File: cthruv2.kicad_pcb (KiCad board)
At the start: 6 copper layers, 27 x 16.4 mm, 10 parts, among them J1 USB_C_Receptacle, J2 Conn_01x03, J3 Conn_01x05, J7 VBUS, J8 Conn_01x05, P1 USB_C_Plug

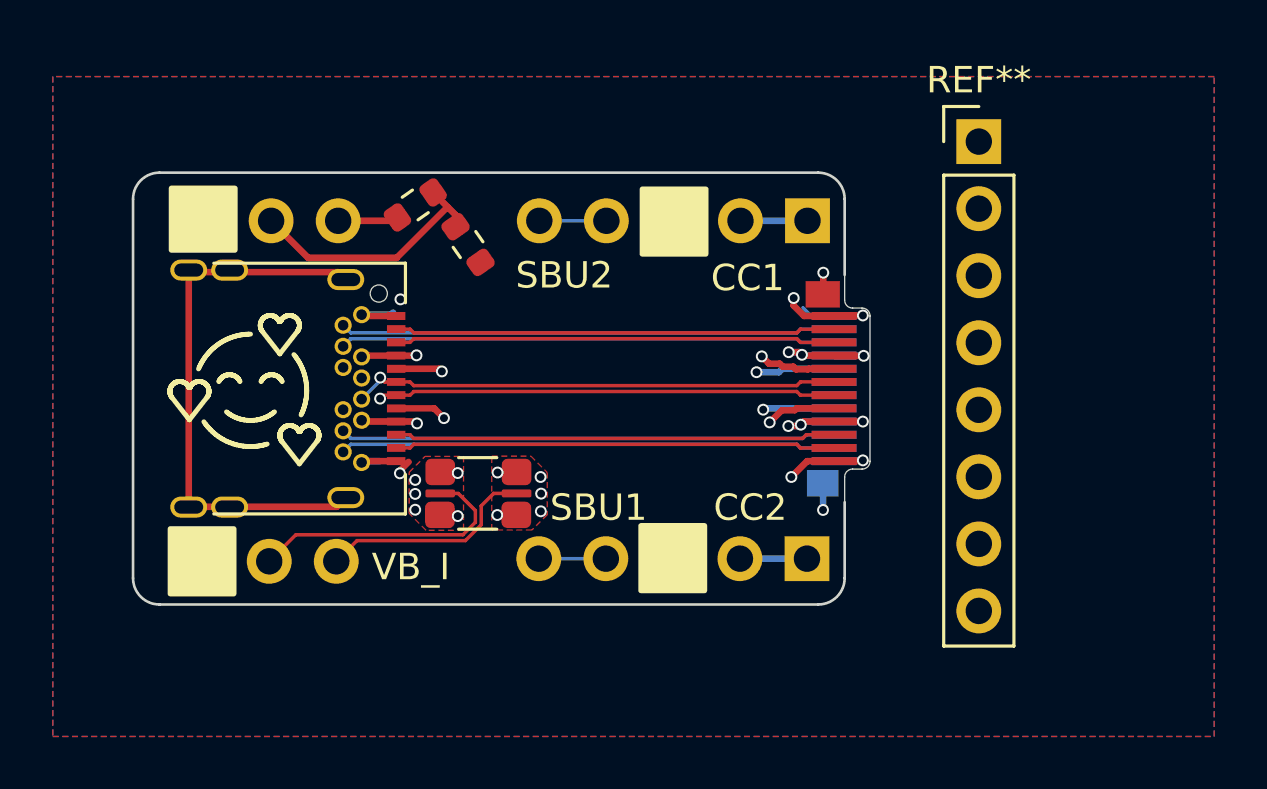
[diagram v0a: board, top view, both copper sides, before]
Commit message: v3: rerouted pin header pinout, improved routing
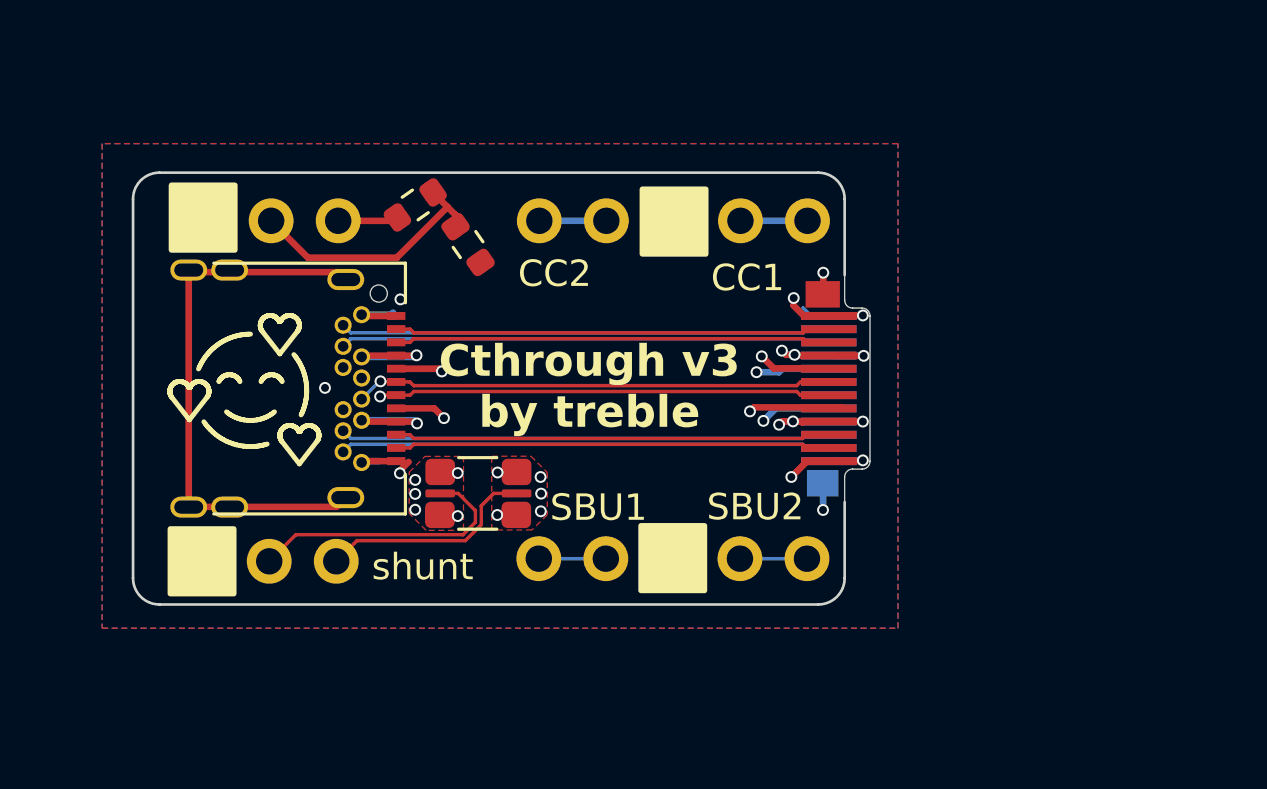
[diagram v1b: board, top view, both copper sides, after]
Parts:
- removed REF**: PinHeader_1x08_P2.54mm_Vertical, Connector_PinHeader_2.54mm:PinHeader_1x08_P2.54mm_Vertical
- P1: footprint USBCPASSTHRU.kicad_pcb:USB_C_Plug_Molex_105444 -> cthruv2:USB_C_Plug_Molex_105444
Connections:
- J1 pad S1: Net-(J1-SHIELD) -> GND
- J3 pad 4: /SBU2 -> /CC2
- J3 pad 5: /SBU2 -> /CC2
- J8 pad 1: /CC2 -> /SBU2
- J8 pad 2: /CC2 -> /SBU2
- P1 pad S1: Net-(J1-SHIELD) -> GND
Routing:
- net Net-(J1-SHIELD): track 23.0 -> 0.00 mm, vias 2 -> 0
- net GND: track 18.1 -> 41.2 mm, vias 6 -> 9
- net /SBU2: track 29.0 -> 38.0 mm
- net /SBU1: track 25.0 -> 29.6 mm
- net VBUS: track 6.55 -> 10.8 mm
- net /VBUS_IN: track 11.6 -> 14.8 mm
- net /CC1: track 27.2 -> 30.0 mm
- net /CC2: track 38.6 -> 36.9 mm
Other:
- board text added: "Cthrough v3 by treble"
- board text added: "Cthrough v3 by treble & Arya"
- board text added: "shunt"
- board text removed: "Cthrough v1 by treble & Arya"
- board text removed: "VB_I"
